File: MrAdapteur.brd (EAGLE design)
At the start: 95 x 45.3 mm, 17 parts, among them X1 1751248, X2 NEB21R

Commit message: Replaced DC connector with the adafruit one for bigger holes
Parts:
- removed X2: NEB21R, con-lumberg:NEB21R
- added U$6: 2.1MMJACKTHM, adafruit:PJ-102A
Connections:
- net N$1: now also U$6.TIP; no longer X2.1
- net N$3: now also U$6.RING, U$6.RING_SW; no longer X2.2, X2.3

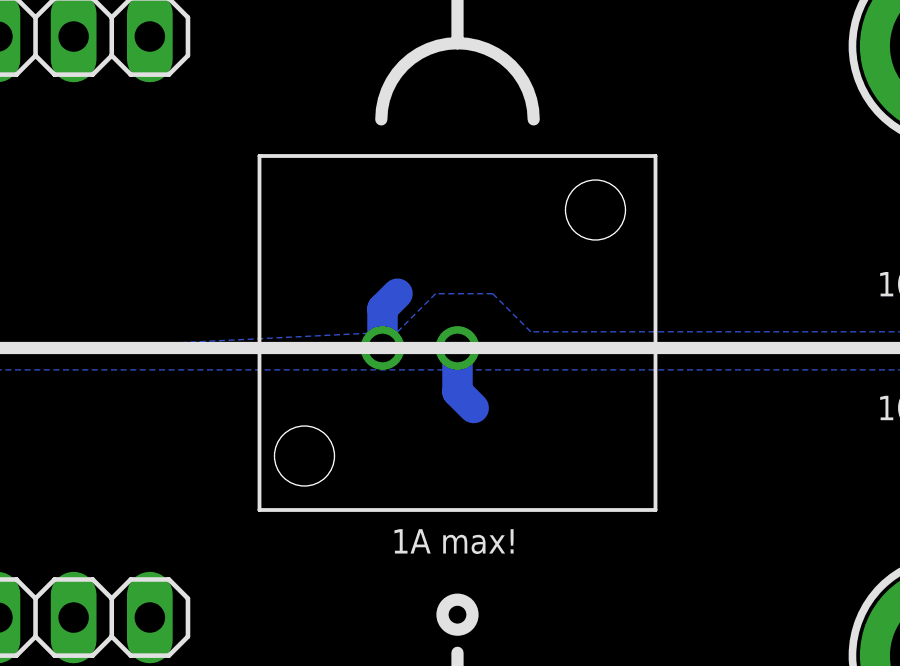
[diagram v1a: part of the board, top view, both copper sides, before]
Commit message: Added larger pads for the BNC connector
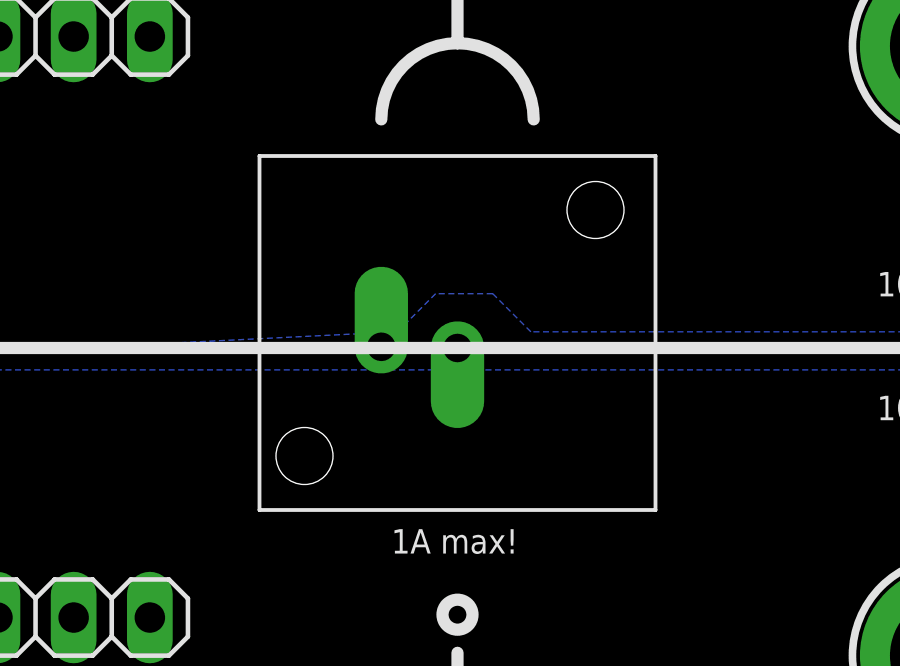
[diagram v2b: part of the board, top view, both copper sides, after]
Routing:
- net N$1: track 2.22 -> 0.00 mm
- net N$3: track 2.02 -> 0.00 mm
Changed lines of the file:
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@@
 <setting verticaltext="up"/>
 </settings>
-<grid distance="0.05" unitdist="inch" unit="inch" style="lines" multiple="1" display="no" altdistance="0.025" altunitdist="inch" altunit="inch"/>
+<grid distance="1.27" unitdist="mm" unit="mm" style="lines" multiple="1" display="no" altdistance="0.025" altunitdist="inch" altunit="inch"/>
 <layers>
 <layer number="1" name="Top" color="4" fill="1" visible="yes" active="yes"/>
@@
 <vertex x="95.25" y="2.54"/>
 </polygon>
-<wire x1="47.72" y1="22.32" x2="47.72" y2="20.86" width="1.016" layer="16"/>
-<wire x1="47.72" y1="20.86" x2="48.26" y2="20.32" width="1.016" layer="16"/>
 <contactref element="U$6" pad="TIP"/>
 </signal>
@@
 <vertex x="13.335" y="17.145"/>
 </polygon>
-<wire x1="45.22" y1="22.32" x2="45.22" y2="23.63" width="1.016" layer="16"/>
-<wire x1="45.22" y1="23.63" x2="45.72" y2="24.13" width="1.016" layer="16"/>
 <contactref element="U$6" pad="RING"/>
 <contactref element="U$6" pad="RING_SW"/>

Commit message: Several minor fixes (sorry, can't remember them) ;)
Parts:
- removed X7, X8: (no value), con-rib:ST4,8
- moved JP3 4.11 mm to (35.0, 12.0)
- moved JP1 4.07 mm to (35.0, 4.50)
- moved JP4 3.97 mm to (35.0, 40.8)
- moved JP2 3.93 mm to (35.0, 33.3)
- moved X3 2.54 mm to (21.6, 8.26)
- moved X6 2.54 mm to (21.6, 37.5)
- moved U$3 2.39 mm to (62.0, 13.2)
- moved U$4 2.15 mm to (62.0, 32.1)
- moved U$1 1.41 mm to (79.0, 13.2)
- moved U$2 0.93 mm to (79.0, 32.1)
- moved U$6 0.40 mm to (4.45, 22.6)
- moved X1 0.40 mm to (91.3, 22.7)
- moved U$5 0.30 mm to (47.7, 22.6)
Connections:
- net N$1: no longer X7.1, X7.2
- net N$3: no longer X8.1, X8.2

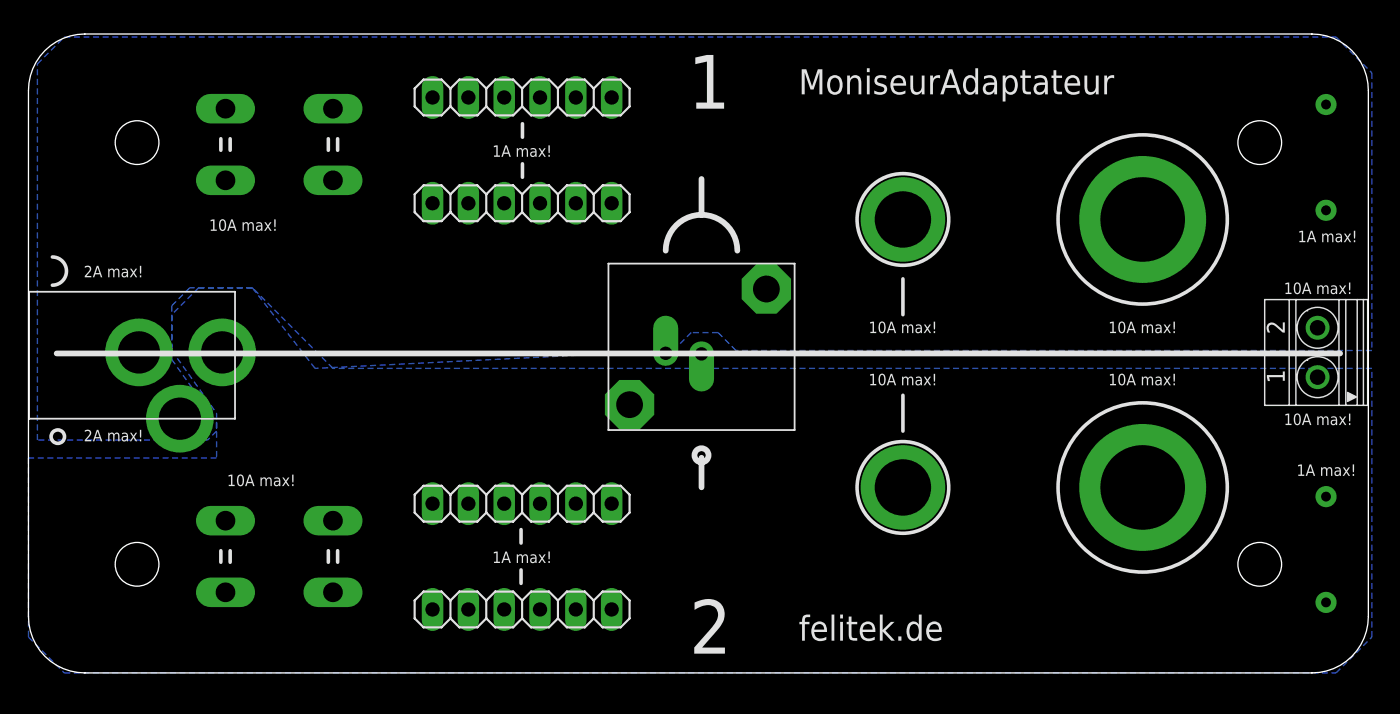
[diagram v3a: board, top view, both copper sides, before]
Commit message: Replaced via with proper solder point
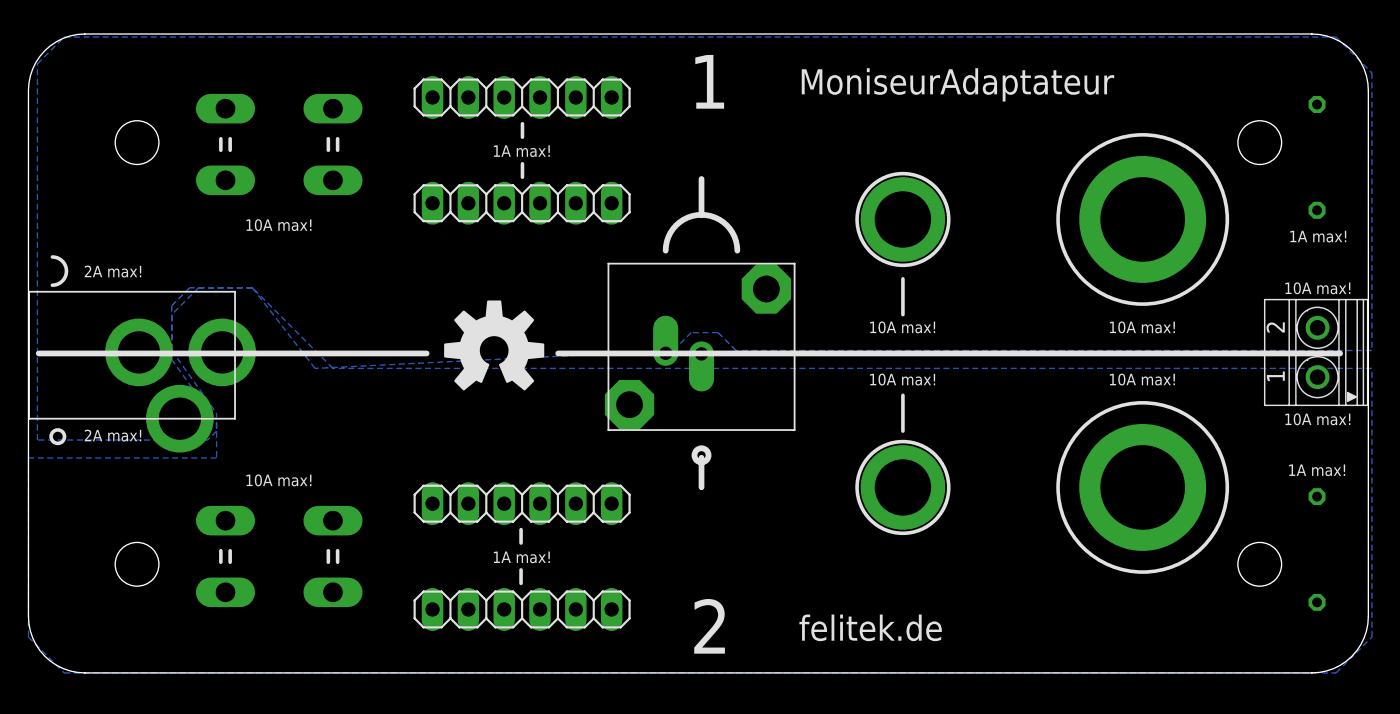
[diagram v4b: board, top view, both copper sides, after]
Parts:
- added U$10, U$11, U$8, U$9: SOLPAD07, 4mm:SOLPAD07
- added U$7: (no value), SparkFun:OSHW-LOGO-L
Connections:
- net N$1: now also U$10.P$1, U$8.P$1
- net N$3: now also U$11.P$1, U$9.P$1
